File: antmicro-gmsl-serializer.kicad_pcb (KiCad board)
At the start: 4 copper layers, 48 x 48 mm, 91 parts, among them J1 Conn_FFC_WE_68715014022, J2 Conn_FAKRA_2FAI-NZSP-PCBB6, U1 AP62301_TSOT, U2 AP62301_TSOT, U3 NCP163ASN330T1G, U4 REF3025AIDBZT, U5 TLV73312PDBVT, U6 MAX9295A, Y1 Resonator_25MHz_ABM8G

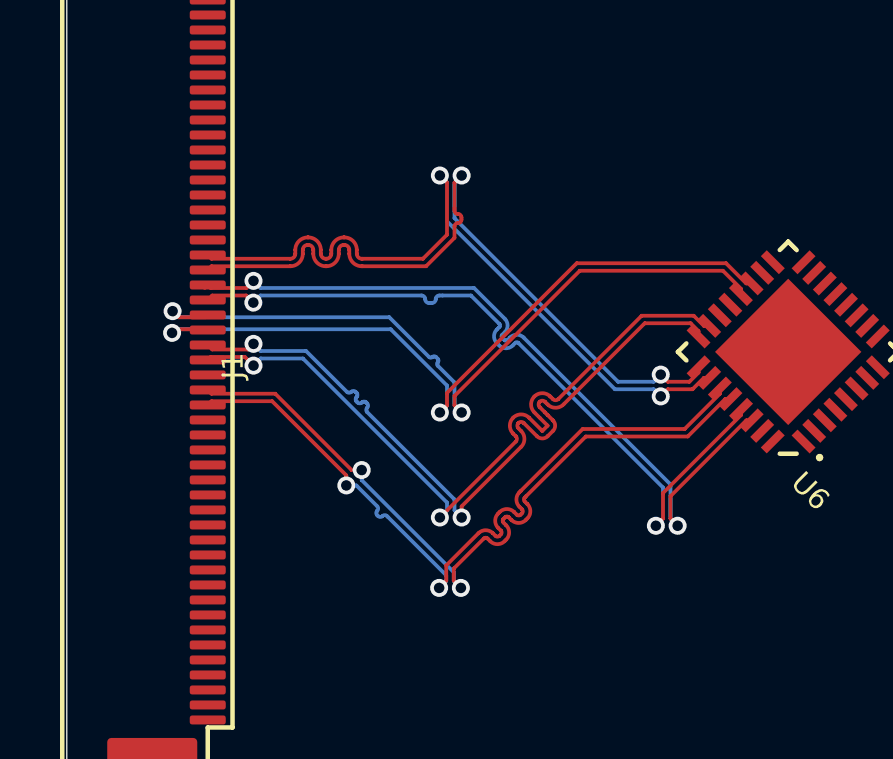
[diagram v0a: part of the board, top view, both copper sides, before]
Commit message: Add stiching vias and GND planes
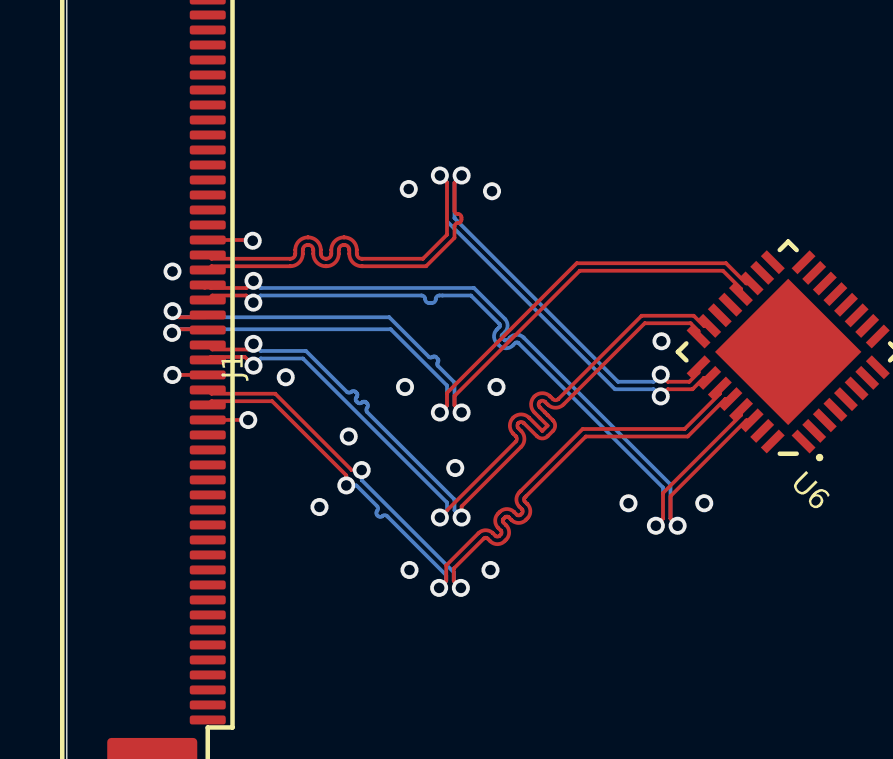
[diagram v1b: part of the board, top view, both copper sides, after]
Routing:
- net GND: track 0.00 -> 4.04 mm, vias 0 -> 17
- added copper zone on In1.Cu, net GND
- added copper zone on In2.Cu, net GND
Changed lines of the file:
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@@
     (style (thickness 0.1) (arrow_length 1.27) (text_position_mode 0) (extension_height 0.58642) (extension_offset 0.5) keep_text_aligned)
   )
+  (segment (start 129.699 104.099) (end 129.7 104.1) (width 0.125) (layer "F.Cu") (net 1))
+  (segment (start 128.35 102.598) (end 127.177 102.598) (width 0.125) (layer "F.Cu") (net 1))
+  (segment (start 128.35 104.099) (end 129.699 104.099) (width 0.125) (layer "F.Cu") (net 1))
+  (segment (start 127.177 102.598) (end 127.175 102.6) (width 0.125) (layer "F.Cu") (net 1))
+  (segment (start 129.825 98.1) (end 129.85 98.125) (width 0.125) (layer "F.Cu") (net 1))
+  (segment (start 128.35 98.1) (end 129.825 98.1) (width 0.125) (layer "F.Cu") (net 1))
+  (via (at 130.95 102.675) (size 0.6) (drill 0.35) (layers "F.Cu" "B.Cu") (net 1))
+  (via (at 142.375 106.875) (size 0.6) (drill 0.35) (layers "F.Cu" "B.Cu") (net 1))
+  (via (at 127.175 102.6) (size 0.6) (drill 0.35) (layers "F.Cu" "B.Cu") (net 1))
+  (via (at 135.05 96.4) (size 0.6) (drill 0.35) (layers "F.Cu" "B.Cu") (net 1))
+  (via (at 132.075 107) (size 0.6) (drill 0.35) (layers "F.Cu" "B.Cu") (net 1))
+  (via (at 127.175 99.15) (size 0.6) (drill 0.35) (layers "F.Cu" "B.Cu") (net 1))
+  (via (at 144.9 106.875) (size 0.6) (drill 0.35) (layers "F.Cu" "B.Cu") (net 1))
+  (via (at 143.475 101.475) (size 0.6) (drill 0.35) (layers "F.Cu" "B.Cu") (net 1))
+  (via (at 134.925 103) (size 0.6) (drill 0.35) (layers "F.Cu" "B.Cu") (net 1))
+  (via (at 136.6 105.7) (size 0.6) (drill 0.35) (layers "F.Cu" "B.Cu") (net 1))
+  (via (at 137.825 96.475) (size 0.6) (drill 0.35) (layers "F.Cu" "B.Cu") (net 1))
+  (via (at 133.05 104.65) (size 0.6) (drill 0.35) (layers "F.Cu" "B.Cu") (net 1))
+  (via (at 137.775 109.1) (size 0.6) (drill 0.35) (layers "F.Cu" "B.Cu") (net 1))
+  (via (at 129.85 98.125) (size 0.6) (drill 0.35) (layers "F.Cu" "B.Cu") (net 1))
+  (via (at 137.975 103) (size 0.6) (drill 0.35) (layers "F.Cu" "B.Cu") (net 1))
+  (via (at 129.7 104.1) (size 0.6) (drill 0.35) (layers "F.Cu" "B.Cu") (net 1))
+  (via (at 135.075 109.1) (size 0.6) (drill 0.35) (layers "F.Cu" "B.Cu") (net 1))
   (segment (start 133.5 98.725) (end 135.523222 98.725) (width 0.125) (layer "F.Cu") (net 37))
   (segment (start 144.508741 103.075) (end 144.888041 102.6957) (width 0.125) (layer "F.Cu") (net 37))
@@
   (arc (start 133.999111 106.975888) (mid 134.029975 107.050403) (end 133.99911 107.124917) (width 0.125) (layer "B.Cu") (net 46))
   (arc (start 134.026859 107.301692) (mid 134.101373 107.332557) (end 134.175887 107.301692) (width 0.125) (layer "B.Cu") (net 46))
+  (zone (net 1) (net_name "GND") (layer "In1.Cu") (hatch edge 0.508)
+    (connect_pads (clearance 0.508))
+    (min_thickness 0.254) (filled_areas_thickness no)
+    (fill yes (thermal_gap 0.508) (thermal_bridge_width 0.508))
+    (polygon
+      (pts
+        (xy 171.65 125.85)
+        (xy 123.65 125.85)
+        (xy 123.65 77.85)
+        (xy 171.65 77.85)
+      )
+    )
+  )
+  (zone (net 1) (net_name "GND") (layer "In2.Cu") (hatch edge 0.508)
+    (connect_pads (clearance 0.508))
+    (min_thickness 0.254) (filled_areas_thickness no)
+    (fill yes (thermal_gap 0.508) (thermal_bridge_width 0.508))
+    (polygon
+      (pts
+        (xy 146.875 110.6)
+        (xy 124.175 110.6)
+        (xy 124.175 94.925)
+        (xy 146.875 94.925)
+      )
+    )
+  )
 )

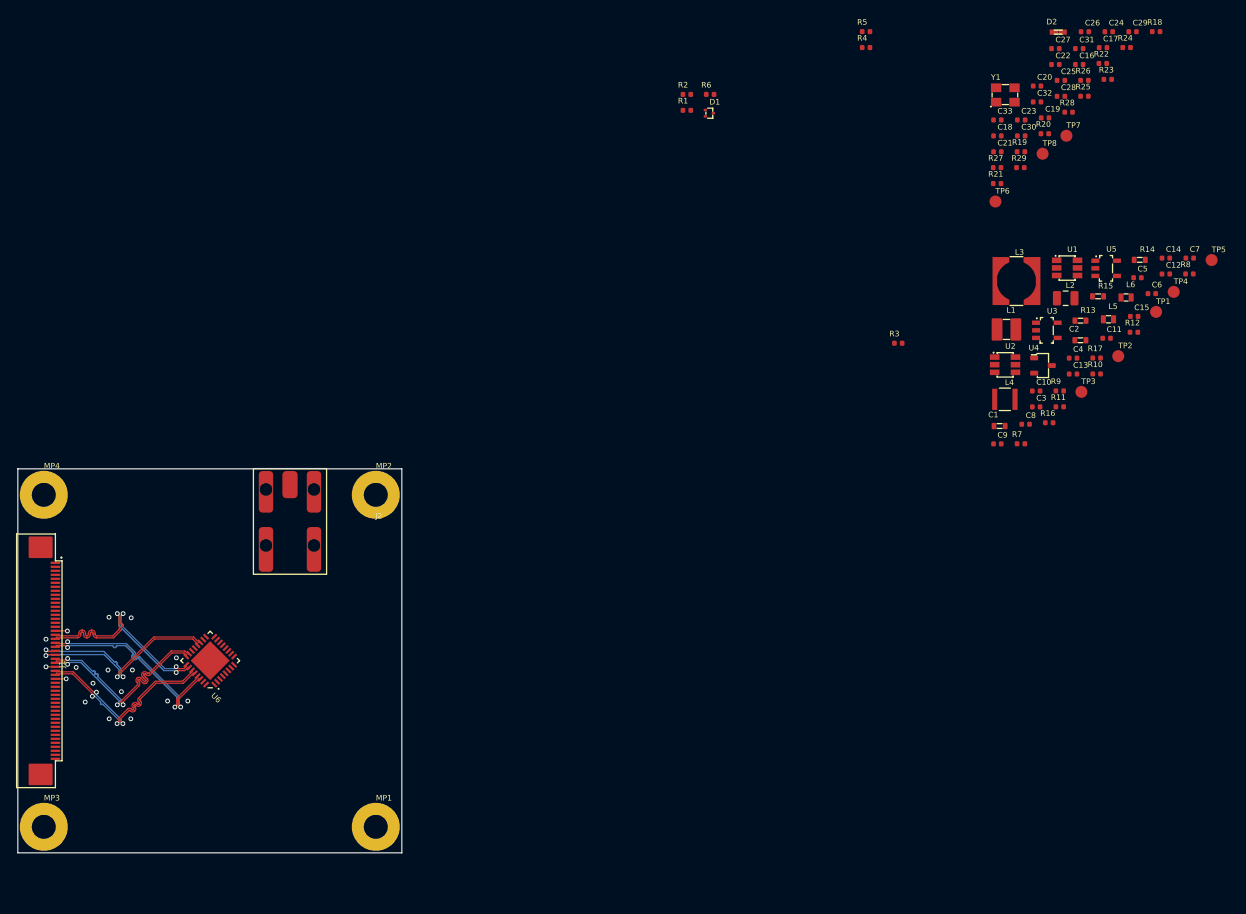
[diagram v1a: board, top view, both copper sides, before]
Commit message: Place and route PoC filter
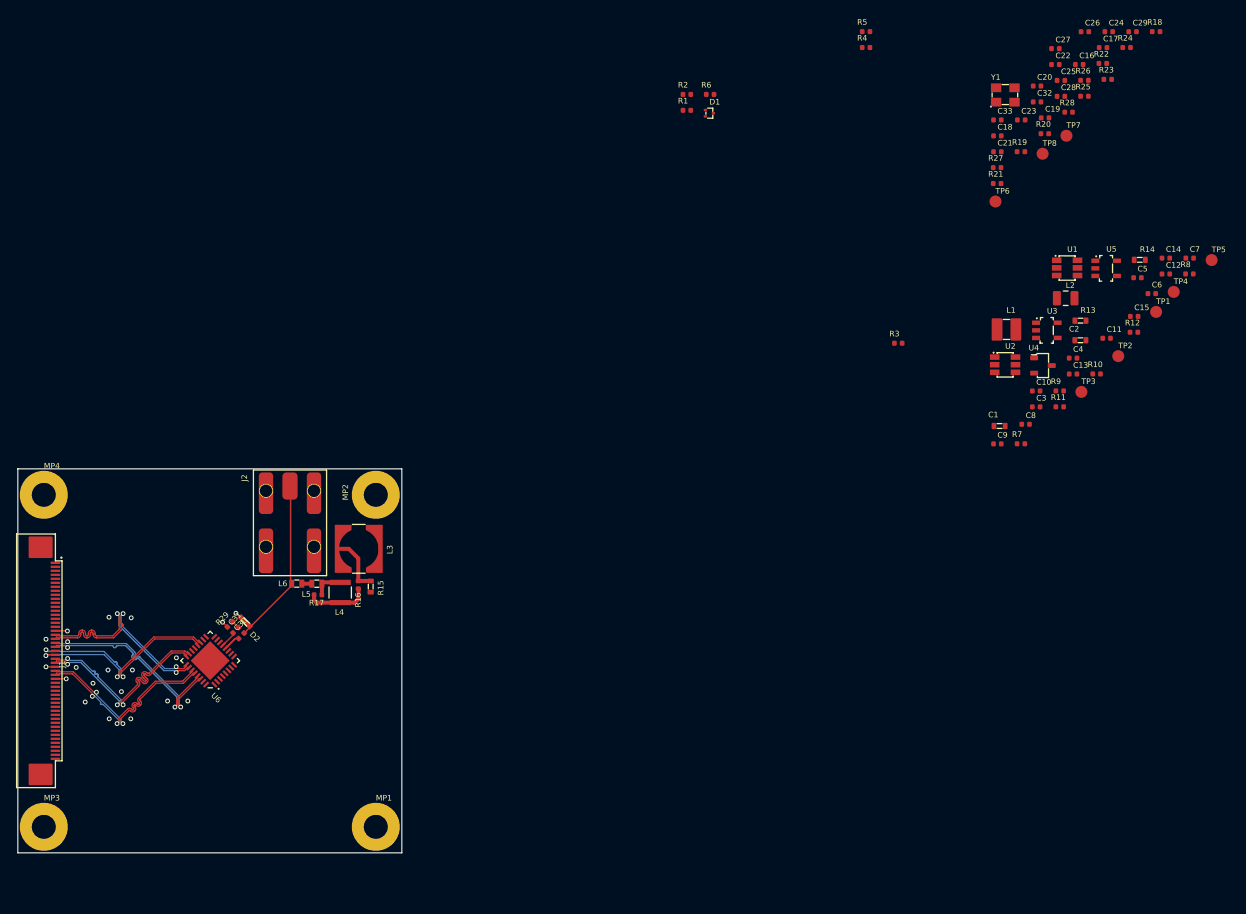
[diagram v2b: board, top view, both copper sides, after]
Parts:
- moved C31 128.1 mm to (150.9, 98.0), turned to 45 degrees
- moved D2 125.5 mm to (152.1, 97.0), turned to 135 degrees
- moved C30 115.8 mm to (151.6, 98.7), turned to 45 degrees
- moved R29 114.1 mm to (150.2, 97.3), turned to 45 degrees
- moved L6 109.7 mm to (158.5, 92.2), turned to 180 degrees
- moved L5 104.3 mm to (161.0, 92.2), turned to 180 degrees
- moved R17 101.7 mm to (161.2, 93.6)
- moved R15 97.9 mm to (167.8, 92.6), turned to 90 degrees
- moved L3 88.8 mm to (166.3, 87.8)
- moved R16 88.7 mm to (166.2, 92.3), turned to -90 degrees
- moved L4 86.5 mm to (163.9, 93.3), turned to 90 degrees
- moved J2 0.17 mm to (157.7, 80.0)
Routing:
- net SIO_P: track 0.00 -> 20.8 mm
- net Net-(L3-Pad2): track 0.00 -> 7.83 mm
- net Net-(L3-Pad1): track 0.00 -> 7.41 mm
- net Net-(L4-Pad2): track 0.00 -> 3.75 mm
- net Net-(C30-Pad1): track 0.00 -> 3.72 mm
- net Net-(C31-Pad1): track 0.00 -> 2.07 mm
- net GND: track 4.04 -> 5.95 mm, vias 17 -> 19
- net Net-(L5-Pad2): track 0.00 -> 1.24 mm
- net Net-(C31-Pad2): track 0.00 -> 1.04 mm

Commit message: Place and route chip decoupling caps and oscillator
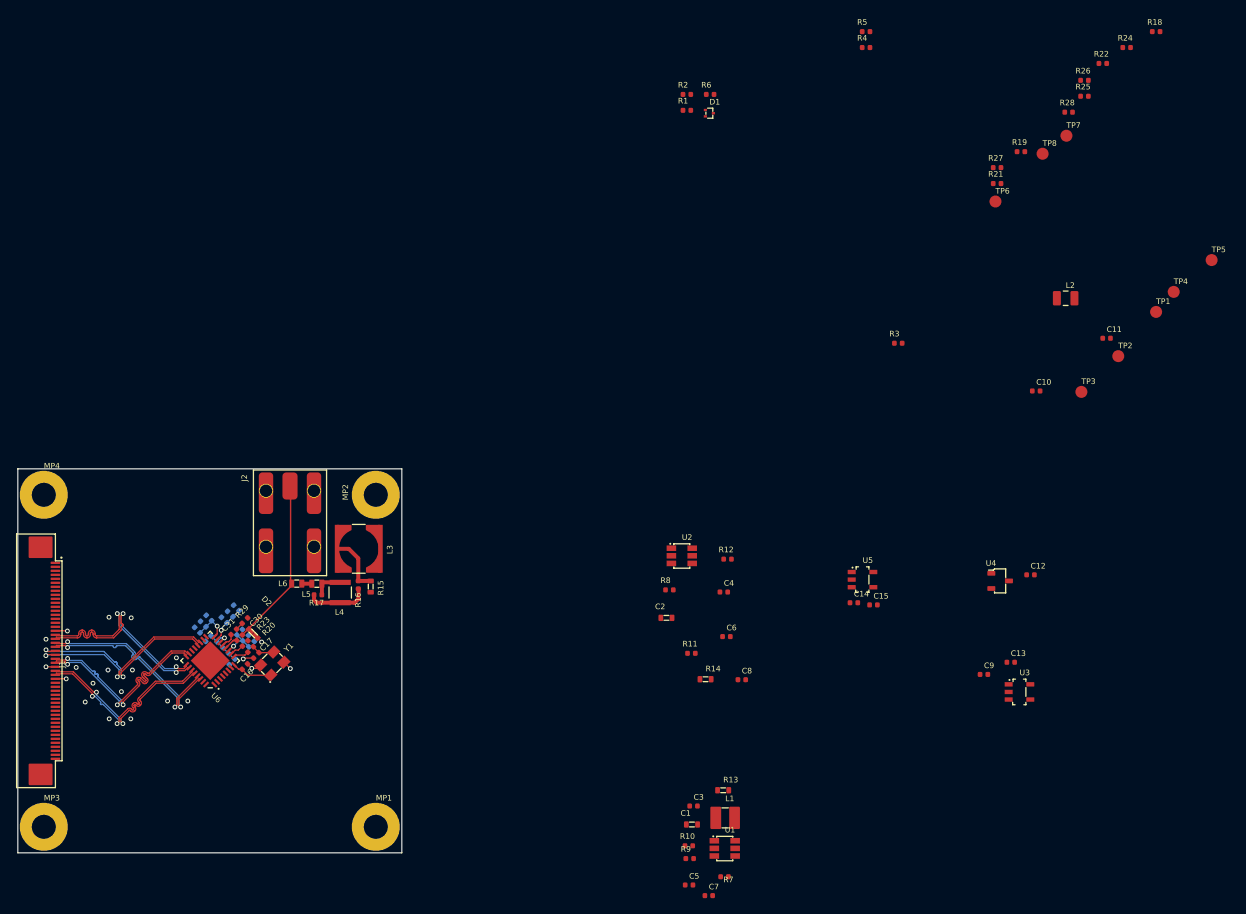
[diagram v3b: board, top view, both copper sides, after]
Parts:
- C18, C19, C20, C21, C22, C23, C24, C25, C26, C27, C28, C29, C32, C33: moved to B.Cu
- moved C29 138.8 mm to (146.1, 98.0), turned to -45 degrees
- moved C24 135.0 mm to (150.4, 102.0), turned to 45 degrees
- moved C26 132.7 mm to (149.7, 101.3), turned to 45 degrees
- moved C17 130.3 mm to (153.5, 101.2), turned to 45 degrees
- moved R23 128.8 mm to (152.1, 99.7), turned to -135 degrees
- moved C16 128.6 mm to (152.0, 102.6), turned to -135 degrees
- moved C27 125.0 mm to (152.9, 99.8), turned to -135 degrees
- moved C22 125.0 mm to (149.4, 96.8), turned to -45 degrees
- moved C25 123.5 mm to (152.1, 99.0), turned to -135 degrees
- moved C19 122.7 mm to (148.9, 100.5), turned to 45 degrees
- moved C28 122.6 mm to (151.4, 98.3), turned to -135 degrees
- moved C32 122.0 mm to (147.5, 96.5), turned to -45 degrees
- moved C20 120.5 mm to (150.2, 96.0), turned to -45 degrees
- moved C23 120.3 mm to (148.2, 99.8), turned to 45 degrees
- moved R20 118.4 mm to (152.8, 100.4), turned to -135 degrees
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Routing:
- net Net-(C19-Pad2): track 0.00 -> 6.11 mm, vias 0 -> 1
- net /Serializer/X1: track 0.00 -> 5.13 mm
- net +1V2: track 0.00 -> 4.77 mm, vias 0 -> 1
- net +3V3: track 0.00 -> 4.56 mm, vias 0 -> 1
- net +1V8: track 0.00 -> 4.48 mm, vias 0 -> 1
- net GND: track 5.95 -> 9.54 mm, vias 19 -> 21
- net /Serializer/X2_R: track 0.00 -> 2.89 mm
- net /Serializer/X2: track 0.00 -> 2.25 mm
- net Net-(C30-Pad1): track 3.72 -> 1.81 mm
- net Net-(R23-Pad2): track 0.00 -> 1.79 mm
